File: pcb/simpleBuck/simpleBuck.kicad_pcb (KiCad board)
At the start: 4 copper layers, 76.2 x 50.8 mm, 79 parts, among them J1 Conn_01x08, J3 Conn_01x04, J4 Conn_01x02, J5 Conn_01x04, J6 Conn_01x02, Q1 TRANSISTOR_PNPMMBT4403, U1 ANALOG_LTC1288CS8#PBF, U2 TI_INA181A2, U3 TI_TL072HIDBVR, U4 TI_TL072HIDBVR, U5 TI_LM4040C41IDBZT, U6 TI_DAC122S085CIMM_NOPB, U7 NATIONALSEMI_LM2596SX-ADJ

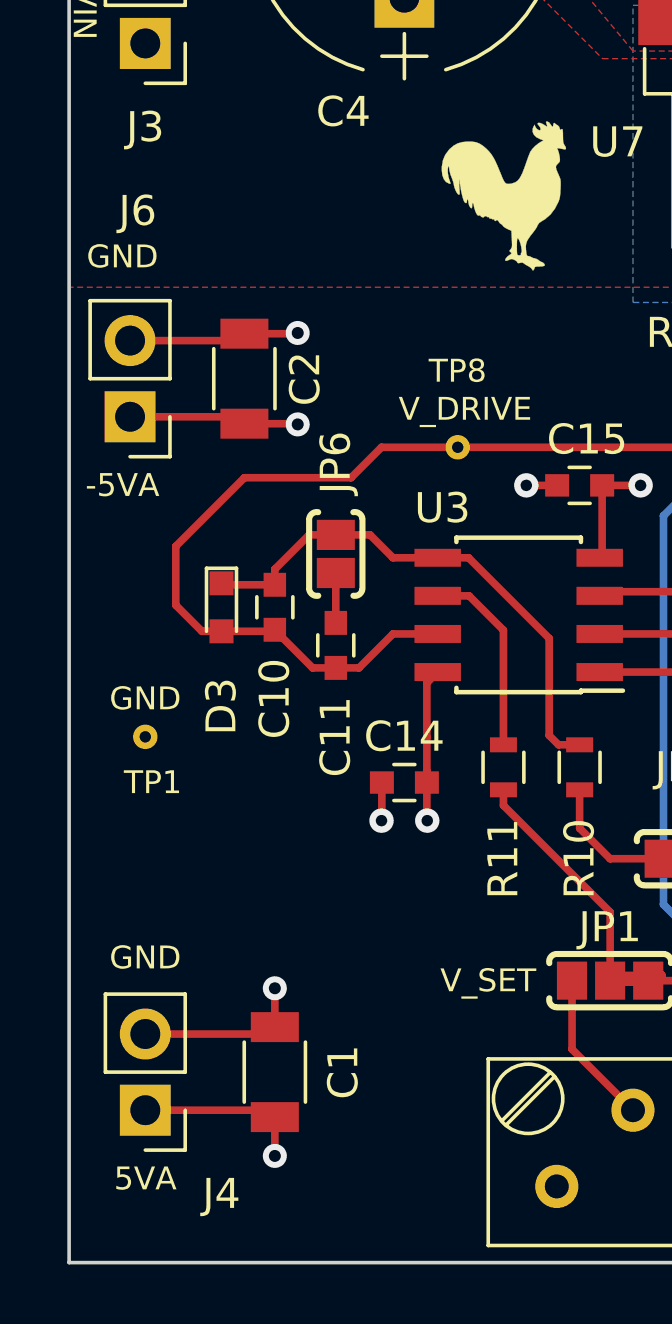
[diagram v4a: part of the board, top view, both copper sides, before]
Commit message: Minor movement of text
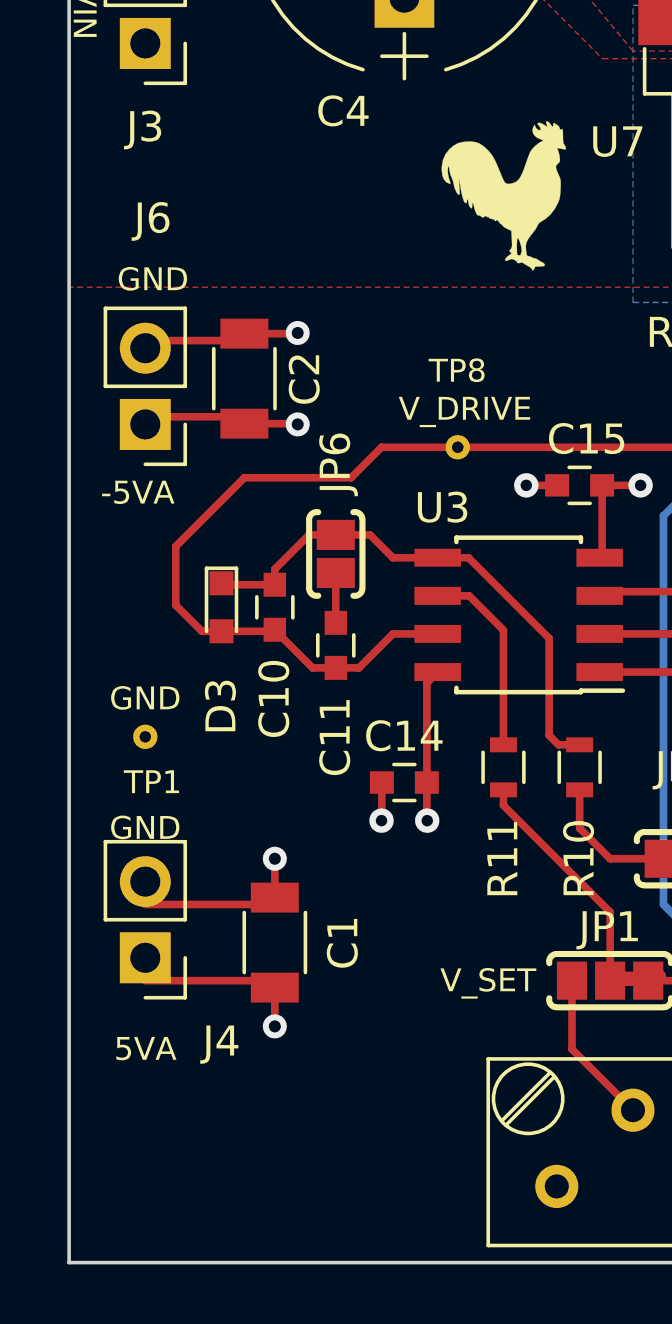
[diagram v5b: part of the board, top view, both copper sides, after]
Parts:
- moved J4 5.08 mm to (916.9, 218.4)
- moved C1 4.32 mm to (921.3, 217.9)
- moved J6 0.57 mm to (916.9, 200.7)
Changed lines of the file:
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@@
   (layers
     (0 F.Cu signal)
-    (1 In1.Cu power hide)
-    (2 In2.Cu power hide)
+    (1 In1.Cu power)
+    (2 In2.Cu power)
     (31 B.Cu signal)
     (32 B.Adhes user)
@@
   )
   (module Pin_Headers:Pin_Header_Straight_1x02_Pitch2.54mm (layer F.Cu)
-    (at 916.432 200.406 180)
+    (at 916.94 200.66 180)
     (descr "Through hole straight pin header, 1x02, 2.54mm pitch, single row")
     (tags "Through hole pin header THT 1x02 2.54mm single row")
@@
   )
   (module Pin_Headers:Pin_Header_Straight_1x02_Pitch2.54mm (layer F.Cu)
-    (at 916.94 223.52 180)
+    (at 916.94 218.44 180)
     (descr "Through hole straight pin header, 1x02, 2.54mm pitch, single row")
     (tags "Through hole pin header THT 1x02 2.54mm single row")
@@
   )
   (module Capacitors_SMD:C_1206 (layer F.Cu)
-    (at 921.258 222.25 90)
+    (at 921.258 217.932 90)
     (descr "Capacitor SMD 1206, reflow soldering, AVX (see smccp.pdf)")
     (tags "capacitor 1206")
@@
     (effects (font (size 1 1) (thickness 0.15)) (justify left))
   )
-  (gr_text -5VA (at 916.178 202.692) (layer F.SilkS)
+  (gr_text -5VA (at 916.686 202.946) (layer F.SilkS)
     (effects (font (size 0.762 0.762) (thickness 0.15)))
   )
-  (gr_text 5VA (at 916.94 225.806) (layer F.SilkS)
+  (gr_text 5VA (at 916.94 221.488) (layer F.SilkS)
     (effects (font (size 0.762 0.762) (thickness 0.15)))
   )
@@
     (effects (font (size 0.762 0.762) (thickness 0.15)))
   )
-  (gr_text GND (at 916.94 218.44) (layer F.SilkS)
+  (gr_text GND (at 916.94 214.122) (layer F.SilkS)
     (effects (font (size 0.762 0.762) (thickness 0.15)))
   )
-  (gr_text GND (at 916.178 195.072) (layer F.SilkS)
+  (gr_text GND (at 917.194 195.834) (layer F.SilkS)
     (effects (font (size 0.762 0.762) (thickness 0.15)))
   )
@@
   (via (at 956.31 213.36) (size 0.8) (drill 0.4) (layers F.Cu B.Cu) (net 1))
   (segment (start 956.437 213.487) (end 956.31 213.36) (width 0.254) (layer F.Cu) (net 1))
-  (segment (start 921.028 220.98) (end 921.258 220.75) (width 0.254) (layer F.Cu) (net 1))
-  (segment (start 916.94 220.98) (end 921.028 220.98) (width 0.254) (layer F.Cu) (net 1))
-  (via (at 921.258 219.456) (size 0.8) (drill 0.4) (layers F.Cu B.Cu) (net 1))
-  (segment (start 921.258 220.75) (end 921.258 219.456) (width 0.254) (layer F.Cu) (net 1))
+  (segment (start 921.028 216.662) (end 921.258 216.432) (width 0.254) (layer F.Cu) (net 1))
+  (segment (start 916.94 216.662) (end 921.028 216.662) (width 0.254) (layer F.Cu) (net 1))
+  (via (at 921.258 215.138) (size 0.8) (drill 0.4) (layers F.Cu B.Cu) (net 1))
+  (segment (start 921.258 216.432) (end 921.258 215.138) (width 0.254) (layer F.Cu) (net 1))
   (via (at 985.012 202.692) (size 0.8) (drill 0.4) (layers F.Cu B.Cu) (net 1))
   (segment (start 985.012 203.974) (end 985.012 202.692) (width 0.254) (layer F.Cu) (net 1))
@@
   (via (at 973.328 211.582) (size 0.8) (drill 0.4) (layers F.Cu B.Cu) (net 1))
   (segment (start 974.356 211.582) (end 973.328 211.582) (width 0.254) (layer F.Cu) (net 1))
-  (segment (start 921.028 223.52) (end 921.258 223.75) (width 0.254) (layer F.Cu) (net 2))
-  (segment (start 916.94 223.52) (end 921.028 223.52) (width 0.254) (layer F.Cu) (net 2))
-  (via (at 921.258 225.044) (size 0.8) (drill 0.4) (layers F.Cu B.Cu) (net 2))
-  (segment (start 921.258 223.75) (end 921.258 225.044) (width 0.254) (layer F.Cu) (net 2))
+  (segment (start 921.028 219.202) (end 921.258 219.432) (width 0.254) (layer F.Cu) (net 2))
+  (segment (start 916.94 219.202) (end 921.028 219.202) (width 0.254) (layer F.Cu) (net 2))
+  (via (at 921.258 220.726) (size 0.8) (drill 0.4) (layers F.Cu B.Cu) (net 2))
+  (segment (start 921.258 219.432) (end 921.258 220.726) (width 0.254) (layer F.Cu) (net 2))
   (segment (start 975.962 211.476) (end 975.856 211.582) (width 0.254) (layer F.Cu) (net 2))
   (segment (start 975.962 209.169) (end 975.962 211.476) (width 0.254) (layer F.Cu) (net 2))
@@
     (polygon
       (pts
-        (xy 990.6 199.136) (xy 990.6 205.994) (xy 914.4 205.994) (xy 914.4 199.136)
+        (xy 990.6 199.644) (xy 990.6 205.994) (xy 914.4 205.994) (xy 914.4 199.644)
       )
     )
@@
     (polygon
       (pts
-        (xy 990.6 198.628) (xy 914.4 198.628) (xy 914.4 177.8) (xy 990.6 177.8)
+        (xy 990.6 199.136) (xy 914.4 199.136) (xy 914.4 177.8) (xy 990.6 177.8)
       )
     )
